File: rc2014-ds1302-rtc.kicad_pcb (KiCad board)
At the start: 2 copper layers, 100 x 50 mm, 16 parts, among them P1 RC2014 BUS, SW1 SW_DIP_x06, U1 74HCT688, U2 74LS125, U3 74LS174, U4 DS1302, U5 74LS32, Y1 Crystal

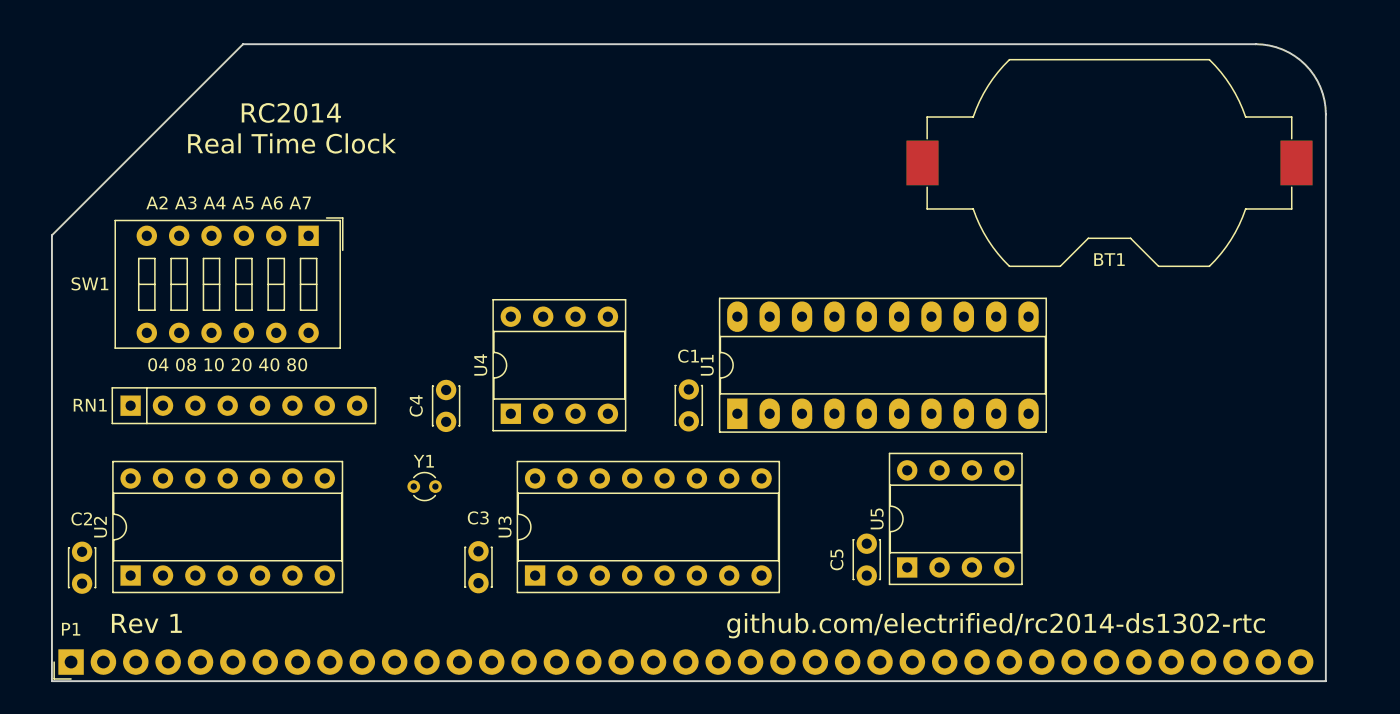
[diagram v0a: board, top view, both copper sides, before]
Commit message: start pcb layout
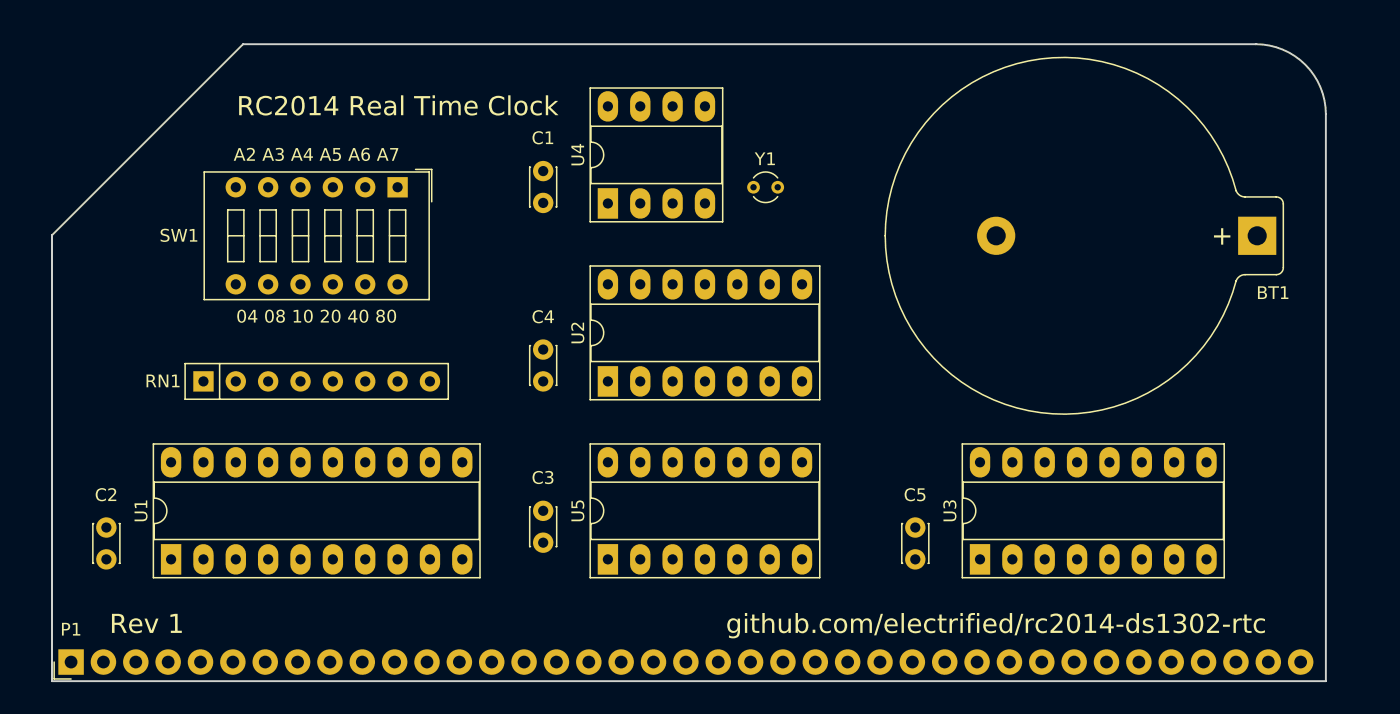
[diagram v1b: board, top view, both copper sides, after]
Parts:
- BT1: footprint Battery_Holders:Keystone_1058_1x2032-CoinCell -> Battery_Holders:Keystone_106_1x20mm-CoinCell
- U2: footprint Housings_DIP:DIP-14_W7.62mm_Socket -> Housings_DIP:DIP-14_W7.62mm_Socket_LongPads
- U3: footprint Housings_DIP:DIP-16_W7.62mm_Socket -> Housings_DIP:DIP-16_W7.62mm_Socket_LongPads
- U4: footprint Housings_DIP:DIP-8_W7.62mm_Socket -> Housings_DIP:DIP-8_W7.62mm_Socket_LongPads
- U5: footprint Housings_DIP:DIP-8_W7.62mm_Socket -> Housings_DIP:DIP-14_W7.62mm_Socket_LongPads
- Y1: footprint Crystals:Crystal_Round_d1.5mm_Vertical -> Crystals:Crystal_Round_d2.0mm_Vertical
- moved REF*** 64.0 mm to (142.2, 129.5)
- moved U1 45.9 mm to (69.8, 154.9)
- moved U2 40.4 mm to (104.1, 141.0)
- moved Y1 35.5 mm to (115.6, 125.7)
- moved U3 34.9 mm to (133.3, 154.9)
- moved U5 23.5 mm to (104.1, 154.9)
- moved C1 20.6 mm to (99.1, 127.0)
- moved U4 18.2 mm to (104.1, 127.0)
- moved BT1 12.9 mm to (155.1, 129.5), turned to 180 degrees
- moved C4 8.26 mm to (99.1, 141.0)
- moved SW1 7.96 mm to (87.6, 125.7)
- moved RN1 6.02 mm to (72.4, 141.0)
- moved C3 5.99 mm to (99.1, 153.6)
- moved C5 4.02 mm to (128.3, 154.9)
- moved C2 2.69 mm to (64.8, 152.4)
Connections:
- net /BUF_Q4 renamed /RTC_CE
- net /BUF_Q5 renamed /RTC_WE
- net /BUF_Q6 renamed /RTC_CLK
- net /BUF_Q7 renamed /RTC_IN
- net /RTC_DQ renamed /RTC_IO
- C4 pad 1: (no net) -> VCC
- C4 pad 2: (no net) -> GND
- U2 pad 10: //RTC_RD -> (no net)
- U2 pad 8: /D6 -> (no net)
- U4 pad 1: (no net) -> VCC

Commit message: wip
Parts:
- moved C4 5.08 mm to (99.1, 135.9)
- moved C3 3.81 mm to (99.1, 149.8)
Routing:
- net GND: track 0.00 -> 208.4 mm, vias 0 -> 5
- net VCC: track 0.00 -> 202.9 mm, vias 0 -> 2
- net /RTC_CE: track 0.00 -> 61.0 mm
- net //IORQ: track 0.00 -> 59.2 mm, vias 0 -> 5
- net Net-(BT1-Pad1): track 0.00 -> 58.4 mm
- net //RTC_WR: track 0.00 -> 49.7 mm
- net /RTC_CLK: track 0.00 -> 48.9 mm
- net //CS_RTC: track 0.00 -> 46.9 mm, vias 0 -> 2
- net /RTC_WE: track 0.00 -> 45.0 mm
- net Net-(RN1-Pad8): track 0.00 -> 42.1 mm
- net /RTC_IO: track 0.00 -> 40.0 mm
- net Net-(RN1-Pad5): track 0.00 -> 37.5 mm
- net //M1: track 0.00 -> 33.1 mm
- net /D0: track 0.00 -> 32.3 mm
- net Net-(RN1-Pad6): track 0.00 -> 26.8 mm, vias 0 -> 1
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
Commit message: after autoroute
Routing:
- net Net-(RN1-Pad7): track 26.7 -> 77.9 mm
- net VCC: track 202.9 -> 164.3 mm, vias 2 -> 0
- net /D5: track 18.9 -> 34.7 mm
- net GND: track 208.4 -> 192.8 mm, vias 5 -> 0
- net Net-(RN1-Pad5): track 37.5 -> 25.8 mm
- net /D6: track 16.6 -> 24.0 mm
- net /RTC_CLK: track 48.9 -> 55.2 mm
- net /A2: track 24.7 -> 18.7 mm
- net //RTC_WR: track 49.7 -> 45.1 mm
- net /D0: track 32.3 -> 37.0 mm
- net /D7: track 23.2 -> 18.7 mm
- net /RTC_WE: track 45.0 -> 40.8 mm
- net Net-(RN1-Pad8): track 42.1 -> 38.0 mm, vias 0 -> 1
- net Net-(BT1-Pad1): track 58.4 -> 55.2 mm
- net //CS_RTC: track 46.9 -> 44.0 mm, vias 2 -> 0
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
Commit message: Think this is ready for manufacturing...
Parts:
- added G***: LOGO, rc2014:clock, B.Cu at (138.4, 130.8)
- added REF**: Via-0.6, rc2014:Via-0.6mm, F.Cu at (127.0, 130.8)
- added REF**: Via-0.6, rc2014:Via-0.6mm, F.Cu at (154.9, 119.4)
- added REF**: Via-0.6, rc2014:Via-0.6mm, F.Cu at (154.9, 142.2)
- added REF**: Via-0.6, rc2014:Via-0.6mm, F.Cu at (154.9, 153.7)
- added REF**: Via-0.6, rc2014:Via-0.6mm, F.Cu at (94.0, 119.4)
- added REF**: Via-0.6, rc2014:Via-0.6mm, F.Cu at (63.5, 158.8)
- added REF**: Via-0.6, rc2014:Via-0.6mm, F.Cu at (73.7, 160.0)
- added REF**: Via-0.6, rc2014:Via-0.6mm, F.Cu at (67.3, 144.8)
- added REF**: Via-0.6, rc2014:Via-0.6mm, F.Cu at (96.5, 158.8)
- added REF**: Via-0.6, rc2014:Via-0.6mm, F.Cu at (127.0, 141.0)
- added REF**: Via-0.6, rc2014:Via-0.6mm, F.Cu at (141.0, 142.2)
- added REF**: Via-0.6, rc2014:Via-0.6mm, F.Cu at (141.0, 119.4)
- added REF**: Via-0.6, rc2014:Via-0.6mm, F.Cu at (63.5, 132.1)
- added REF**: Via-0.6, rc2014:Via-0.6mm, F.Cu at (94.0, 142.2)
- added REF**: Via-0.6, rc2014:Via-0.6mm, F.Cu at (94.0, 132.1)
- added REF**: Via-0.6, rc2014:Via-0.6mm, F.Cu at (81.3, 119.4)
- added REF**: Via-0.6, rc2014:Via-0.6mm, F.Cu at (123.2, 154.9)
- U2: value 74LS125 -> 74HCT125
- U3: value 74LS174 -> 74HCT174
- U5: value 74LS32 -> 74HCT32
- moved REF*** 73.7 mm to (68.6, 132.1)
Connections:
- U2 pad 10: (no net) -> GND
- U2 pad 12: (no net) -> GND
- U2 pad 13: (no net) -> GND
- U2 pad 9: (no net) -> GND
- U5 pad 10: (no net) -> GND
- U5 pad 12: (no net) -> GND
- U5 pad 13: (no net) -> GND
- U5 pad 9: (no net) -> GND
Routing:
- net GND: track 192.8 -> 45.8 mm
- net Net-(RN1-Pad7): track 77.9 -> 72.2 mm
- net /D5: track 34.7 -> 36.8 mm
- net Net-(U4-Pad2): track 10.8 -> 12.3 mm
- net /RTC_CE: track 60.5 -> 62.0 mm
- net /A7: track 13.3 -> 14.8 mm
- net /RTC_WE: track 40.8 -> 41.8 mm
- net /D6: track 24.0 -> 25.0 mm
- net /D0: track 37.0 -> 37.7 mm
- net /A6: track 11.1 -> 11.8 mm
- net /RTC_CLK: track 55.2 -> 55.9 mm
- net VCC: track 164.3 -> 164.9 mm
- added copper zone on B.Cu, net GND
- added copper zone on F.Cu, net GND
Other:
- board text added: "Real Time Clock"
- board text removed: "RC2014 Real Time Clock"

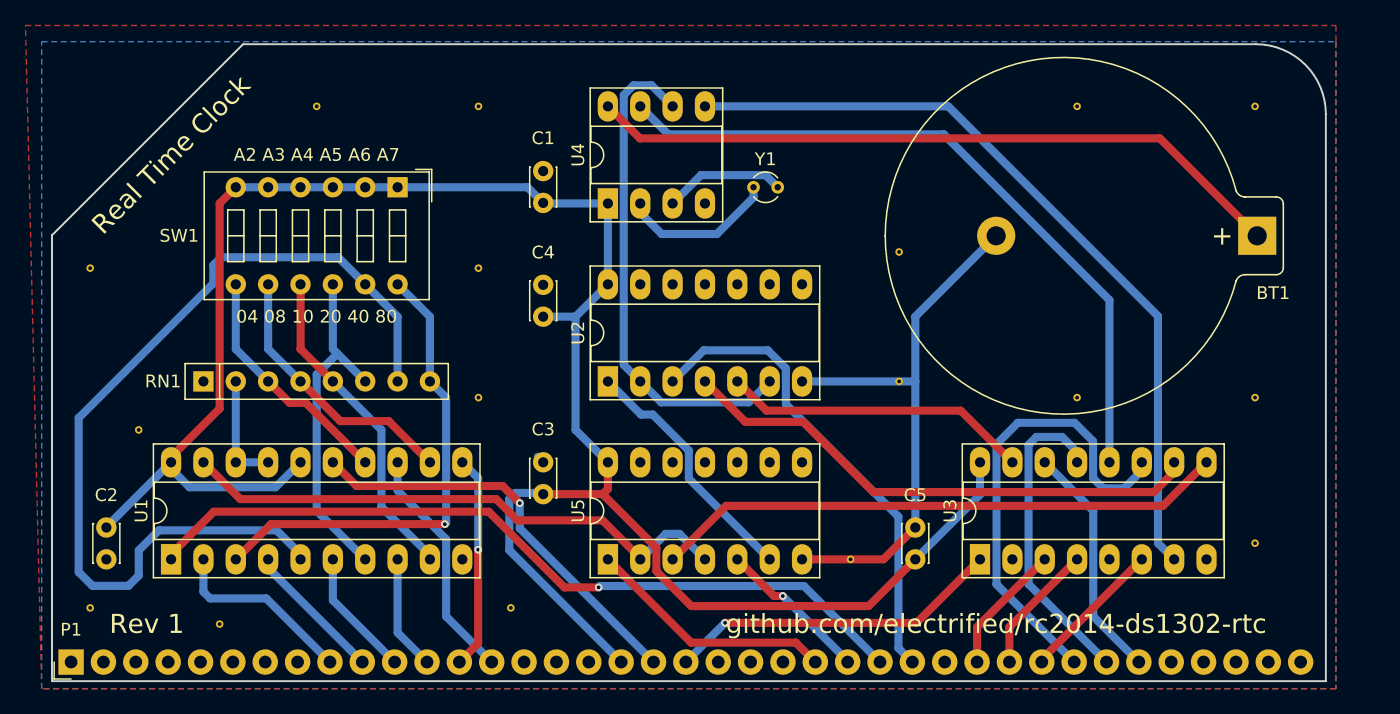
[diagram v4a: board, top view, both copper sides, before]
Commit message: Start kicad 6 migration
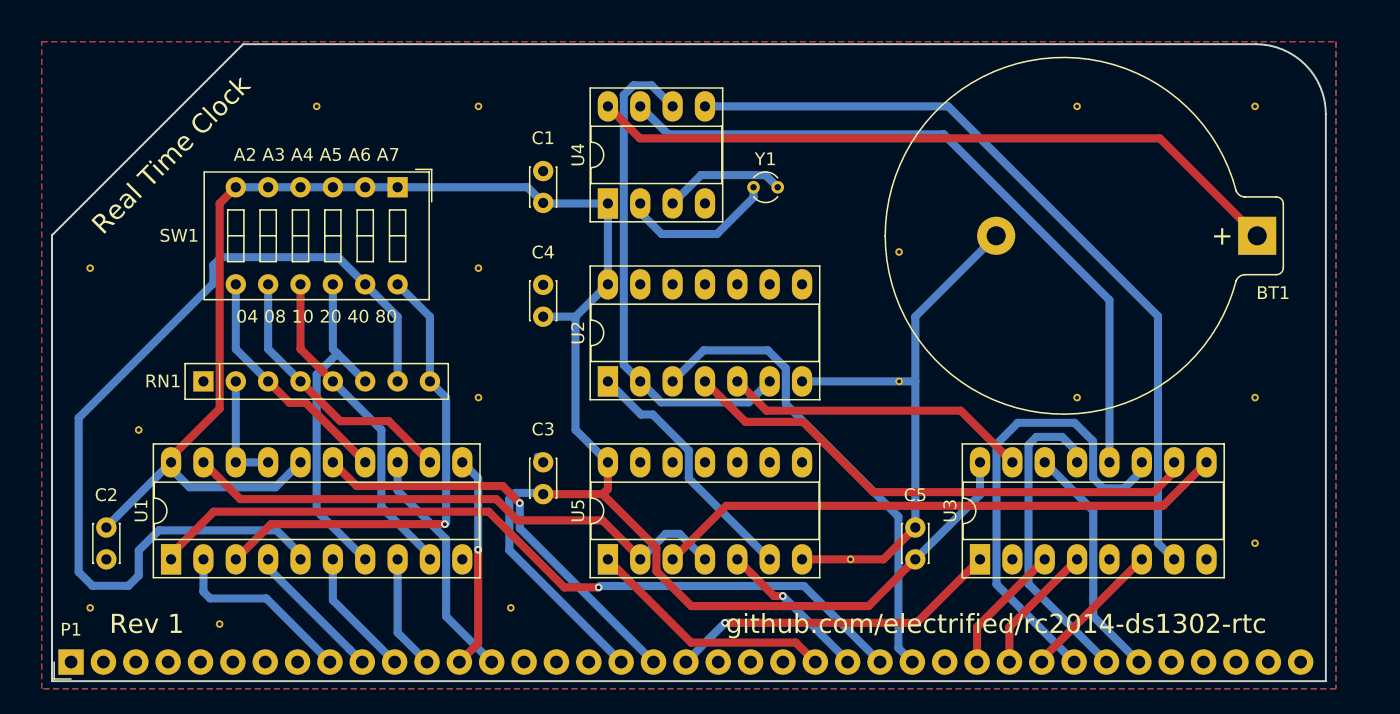
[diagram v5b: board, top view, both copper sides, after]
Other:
- net class Default removed
- net class Power removed

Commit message: Complete kicad 6 migration
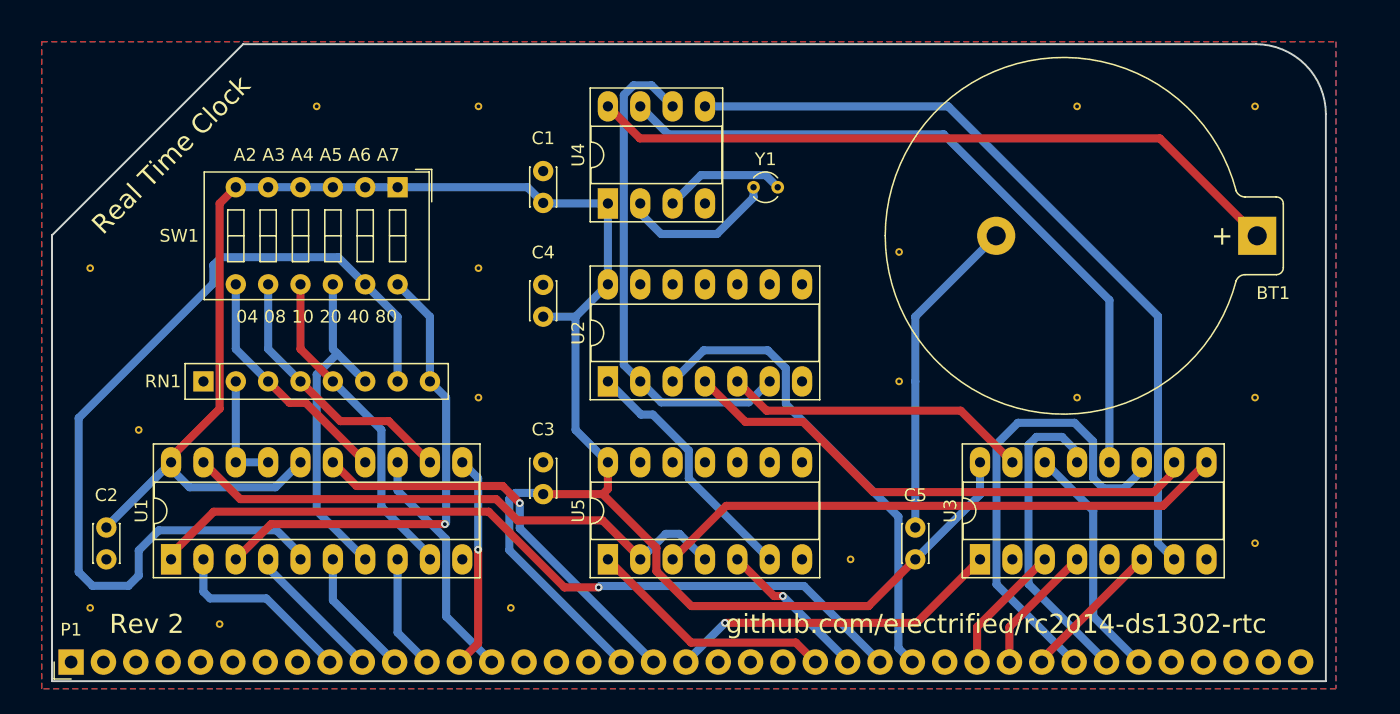
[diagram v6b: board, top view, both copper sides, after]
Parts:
- BT1: footprint Battery_Holders:Keystone_106_1x20mm-CoinCell -> Battery:BatteryHolder_Keystone_106_1x20mm
- U1: footprint Housings_DIP:DIP-20_W7.62mm_Socket_LongPads -> Package_DIP:DIP-20_W7.62mm_Socket_LongPads
- U2, U5: footprint Housings_DIP:DIP-14_W7.62mm_Socket_LongPads -> Package_DIP:DIP-14_W7.62mm_Socket_LongPads
- U3: footprint Housings_DIP:DIP-16_W7.62mm_Socket_LongPads -> Package_DIP:DIP-16_W7.62mm_Socket_LongPads
- U4: value DS1302 -> DS1302+; footprint Housings_DIP:DIP-8_W7.62mm_Socket_LongPads -> Package_DIP:DIP-8_W7.62mm_Socket_LongPads
- Y1: footprint Crystals:Crystal_Round_d2.0mm_Vertical -> Crystal:Crystal_Round_D2.0mm_Vertical
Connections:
- net //CS_RTC renamed //CS_RTC
- net //IORQ renamed //IORQ
- net //M1 renamed //M1
- net //RD renamed //RD
- net //RESET renamed //RESET
- net //RTC_RD renamed //RTC_RD
- net //RTC_WR renamed //RTC_WR
- net //WR renamed //WR
- P1 pad 1: (no net) -> unconnected-(P1-Pad1)
- P1 pad 15: (no net) -> unconnected-(P1-Pad15)
- P1 pad 16: (no net) -> unconnected-(P1-Pad16)
- P1 pad 2: (no net) -> unconnected-(P1-Pad2)
- P1 pad 21: (no net) -> unconnected-(P1-Pad21)
- P1 pad 22: (no net) -> unconnected-(P1-Pad22)
- P1 pad 23: (no net) -> unconnected-(P1-Pad23)
- P1 pad 28: (no net) -> unconnected-(P1-Pad28)
- P1 pad 3: (no net) -> unconnected-(P1-Pad3)
- P1 pad 35: (no net) -> unconnected-(P1-Pad35)
- P1 pad 36: (no net) -> unconnected-(P1-Pad36)
- P1 pad 37: (no net) -> unconnected-(P1-Pad37)
- P1 pad 38: (no net) -> unconnected-(P1-Pad38)
- P1 pad 39: (no net) -> unconnected-(P1-Pad39)
- P1 pad 4: (no net) -> unconnected-(P1-Pad4)
- P1 pad 5: (no net) -> unconnected-(P1-Pad5)
- P1 pad 6: (no net) -> unconnected-(P1-Pad6)
- P1 pad 7: (no net) -> unconnected-(P1-Pad7)
- P1 pad 8: (no net) -> unconnected-(P1-Pad8)
- U2 pad 11: (no net) -> unconnected-(U2-Pad11)
- U2 pad 8: (no net) -> unconnected-(U2-Pad8)
- U3 pad 2: (no net) -> unconnected-(U3-Pad2)
- U3 pad 5: (no net) -> unconnected-(U3-Pad5)
- U5 pad 11: (no net) -> unconnected-(U5-Pad11)
- U5 pad 8: (no net) -> unconnected-(U5-Pad8)
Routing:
- net GND: track 45.8 -> 25.5 mm
- net /A6: track 11.8 -> 10.5 mm
- net VCC: track 164.9 -> 163.7 mm
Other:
- board text added: "Rev 2"
- board text removed: "Rev 1"
